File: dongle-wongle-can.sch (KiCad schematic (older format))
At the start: 33 parts

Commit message: updated project layout
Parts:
- removed U?: AP1509-33, symbol star-sch-block-symbols:AP1509-33
- added U?: AP1509-33, symbol hardware-sch-blocks:AP1509-33
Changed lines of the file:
@@
 Text Notes 6350 3050 0    50   ~ 0
 POWER
-Wire Wire Line
-	6800 4750 7100 4750
 $Comp
-L star-sch-block-symbols:AP1509-33 U?
-U 1 1 5F0A0CB9
+L hardware-sch-blocks:AP1509-33 U?
+U 1 1 5EA62ACD
 P 7300 4300
 F 0 "U?" H 7744 4271 50  0000 L CNN
@@
 $EndComp
 Wire Wire Line
+	6800 4750 7100 4750
+Wire Wire Line
 	7500 4750 7800 4750
-Wire Wire Line
-	7500 4750 7400 4750
-Connection ~ 7500 4750
-Wire Wire Line
-	7400 4750 7300 4750
-Connection ~ 7400 4750
 Wire Wire Line
 	7100 4750 7200 4750
 Connection ~ 7100 4750
+Wire Wire Line
+	7200 4750 7300 4750
 Connection ~ 7200 4750
 Wire Wire Line
-	7200 4750 7300 4750
+	7300 4750 7400 4750
 Connection ~ 7300 4750
+Wire Wire Line
+	7400 4750 7500 4750
+Connection ~ 7400 4750
+Connection ~ 7500 4750
 $EndSCHEMATC

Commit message: updated footprints
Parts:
- C1, C2, C3, C4, C5, C6, C7: renamed from C?; footprint (none) -> Capacitor_SMD:C_0603_1608Metric
- D1: renamed from D?; footprint (none) -> Diode_SMD:D_0603_1608Metric
- D2: renamed from D?; footprint (none) -> LED_SMD:LED_0603_1608Metric_Castellated
- J1: renamed from J?; footprint (none) -> hardware-sch-blocks:505448-0871
- J2, J3: renamed from J?; footprint (none) -> Connector_PinHeader_2.54mm:PinHeader_1x12_P2.54mm_Vertical
- J4: renamed from J?; footprint (none) -> hardware-sch-blocks:TSM-103-01-L-SV
- J5: renamed from J?; footprint (none) -> hardware-sch-blocks:FTMH-120-03-F-DV-P
- JP1: renamed from JP?; footprint (none) -> Jumper:SolderJumper-2_P1.3mm_Open_Pad1.0x1.5mm
- JP2, JP3, JP4: renamed from JP?; footprint (none) -> Jumper:SolderJumper-3_P1.3mm_Bridged2Bar12_Pad1.0x1.5mm
- L1: renamed from L?; footprint (none) -> Inductor_SMD:L_0603_1608Metric
- R1, R2, R3, R4, R5, R6: renamed from R?; footprint (none) -> Resistor_SMD:R_0603_1608Metric
- RN1: renamed from RN?; footprint (none) -> Resistor_SMD:R_Array_Concave_4x0603
- RN2: renamed from RN?; footprint (none) -> Resistor_SMD:R_Array_Concave_2x0603
- SW1: renamed from SW?; footprint (none) -> Button_Switch_SMD:SW_SPST_CK_RS282G05A3
- TP1, TP2: renamed from TP?; footprint (none) -> TestPoint:TestPoint_Keystone_5005-5009_Compact
- U3: renamed from U?; footprint (none) -> Package_SO:SOIC-8_3.9x4.9mm_P1.27mm
- gave numbers to parts that had none: 2
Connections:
- net VDD: now also C7.1
- net at C6.2, D1.2 (A), U3.4 (SD)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: now also C7.2
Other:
- moved on the sheet: C7

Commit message: add layout
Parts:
- removed J2: PROTO_IO, Connector_PinHeader_2.54mm:PinHeader_1x12_P2.54mm_Vertical, symbol Connector_Generic:Conn_02x06_Counter_Clockwise
- removed J3: PROTO_POWER, Connector_PinHeader_2.54mm:PinHeader_1x12_P2.54mm_Vertical, symbol Connector_Generic:Conn_02x06_Counter_Clockwise
- removed JP1: BOOT_JUMP, Jumper:SolderJumper-2_P1.3mm_Open_Pad1.0x1.5mm, symbol Jumper:SolderJumper_2_Open
- removed TP1: CANH_TP, TestPoint:TestPoint_Keystone_5005-5009_Compact, symbol Connector:TestPoint
- removed TP2: CANL_TP, TestPoint:TestPoint_Keystone_5005-5009_Compact, symbol Connector:TestPoint
- added H1, H2, H3, H4: MountingHole, MountingHole:MountingHole_3mm, symbol Mechanical:MountingHole
- added J2: PROTO_IO, Connector_PinHeader_2.54mm:PinHeader_2x06_P2.54mm_Vertical, symbol Connector_Generic:Conn_02x06_Odd_Even
- added J3: PROTO_PWR, hardware-sch-blocks:PROTO_2x6, symbol Connector_Generic:Conn_02x06_Odd_Even
- added J6: PROTO1, hardware-sch-blocks:PROTO_2x6, symbol Connector_Generic:Conn_02x06_Odd_Even
- added J7: PROTO2, hardware-sch-blocks:PROTO_2x6, symbol Connector_Generic:Conn_02x06_Odd_Even
- J5: footprint hardware-sch-blocks:FTMH-120-03-F-DV-P -> hardware-sch-blocks:FTSH-105-01-L-DV-K
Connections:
- net CAN_RX: now also R2.2
- net GND: now also C6.2, C7.2, D1.2 (A), U3.4 (SD), U3.5 (GND), U3.6 (GND), U3.7 (GND), U3.8 (GND), J3.1 (Pin_1), J3.11 (Pin_11), J3.3 (Pin_3), J3.5 (Pin_5), J3.7 (Pin_7), J3.9 (Pin_9)
- net GPIO0: now also J2.2 (Pin_2)
- net GPIO1: now also J2.1 (Pin_1)
- net I2C_SCL: now also J2.8 (Pin_8)
- net I2C_SDA: now also J2.10 (Pin_10)
- net SWDCLK: now also J2.11 (Pin_11)
- net SWDIO: now also J2.12 (Pin_12)
- net UART_RX: now also J2.4 (Pin_4)
- net UART_TX: now also J2.6 (Pin_6)
- net VDD: now also J3.10 (Pin_10), J3.12 (Pin_12), J3.2 (Pin_2), J3.4 (Pin_4), J3.6 (Pin_6), J3.8 (Pin_8)
- net at RN1.5 (R4.2): now also J2.9 (Pin_9)
- net at RN1.6 (R3.2): now also J2.7 (Pin_7)
- net at RN1.7 (R2.2): now also J2.5 (Pin_5)
- net at RN1.8 (R1.2): now also J2.3 (Pin_3)
- no-connect marks 2 -> 26
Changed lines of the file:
@@
 F 0 "J5" H 5700 6700 50  0000 R CNN
 F 1 "Conn_ARM_JTAG_SWD_10" V 5550 6600 50  0000 R CNN
-F 2 "hardware-sch-blocks:FTMH-120-03-F-DV-P" H 6000 6150 50  0001 C CNN
+F 2 "hardware-sch-blocks:FTSH-105-01-L-DV-K" H 6000 6150 50  0001 C CNN
 F 3 "http://infocenter.arm.com/help/topic/com.arm.doc.ddi0314h/DDI0314H_coresight_components_trm.pdf" V 5650 4900 50  0001 C CNN
 	1    6000 6150
@@
 Text GLabel 1600 4550 2    50   Input ~ 0
 CANL
-Wire Wire Line
-	1100 4600 1100 4550
 Wire Wire Line
 	1100 4300 1100 4250
@@
 Wire Wire Line
 	7450 3700 7600 3700
-$Comp
-L Connector:TestPoint TP1
-U 1 1 5EB87845
-P 1100 4200
-F 0 "TP1" H 1158 4318 50  0000 L CNN
-F 1 "CANH_TP" H 1158 4227 50  0000 L CNN
-F 2 "TestPoint:TestPoint_Keystone_5005-5009_Compact" H 1300 4200 50  0001 C CNN
-F 3 "~" H 1300 4200 50  0001 C CNN
-	1    1100 4200
-	1    0    0    -1
-$EndComp
-$Comp
-L Connector:TestPoint TP2
-U 1 1 5EB8AE14
-P 1100 4600
-F 0 "TP2" H 1042 4626 50  0000 R CNN
-F 1 "CANL_TP" H 1042 4717 50  0000 R CNN
-F 2 "TestPoint:TestPoint_Keystone_5005-5009_Compact" H 1300 4600 50  0001 C CNN
-F 3 "~" H 1300 4600 50  0001 C CNN
-	1    1100 4600
-	-1   0    0    1
-$EndComp
 Wire Wire Line
 	1100 4550 1600 4550
-Connection ~ 1100 4550
 Wire Wire Line
 	1100 4550 1100 4500
 Wire Wire Line
 	1600 4250 1100 4250
-Connection ~ 1100 4250
-Wire Wire Line
-	1100 4250 1100 4200
 $Comp
 L Device:C_Small C2
@@
 $EndComp
 Wire Wire Line
-	1200 7300 1350 7300
-Wire Wire Line
 	1000 7300 900  7300
-Wire Wire Line
-	1650 7300 1750 7300
 Wire Wire Line
 	1750 7300 1750 7050
 Connection ~ 1750 7050
-$Comp
-L Jumper:SolderJumper_2_Open JP1
-U 1 1 5EC6FD0B
-P 1500 7300
-F 0 "JP1" H 1500 7200 50  0000 C CNN
-F 1 "BOOT_JUMP" H 1500 7414 50  0000 C CNN
-F 2 "Jumper:SolderJumper-2_P1.3mm_Open_Pad1.0x1.5mm" H 1500 7300 50  0001 C CNN
-F 3 "~" H 1500 7300 50  0001 C CNN
-	1    1500 7300
-	1    0    0    -1
-$EndComp
-$Comp
-L Connector_Generic:Conn_02x06_Counter_Clockwise J3
-U 1 1 5ECB63F8
-P 3550 2050
-F 0 "J3" H 3600 2467 50  0000 C CNN
-F 1 "PROTO_POWER" H 3600 2376 50  0000 C CNN
-F 2 "Connector_PinHeader_2.54mm:PinHeader_1x12_P2.54mm_Vertical" H 3550 2050 50  0001 C CNN
-F 3 "~" H 3550 2050 50  0001 C CNN
-	1    3550 2050
-	1    0    0    -1
-$EndComp
 $Comp
 L power:GND #PWR0125
@@
 Text GLabel 1300 2350 0    50   Input ~ 0
 SWDCLK
-$Comp
-L Connector_Generic:Conn_02x06_Counter_Clockwise J2
-U 1 1 5ECFB1DE
-P 2200 2050
-F 0 "J2" H 2250 2467 50  0000 C CNN
-F 1 "PROTO_IO" H 2250 2376 50  0000 C CNN
-F 2 "Connector_PinHeader_2.54mm:PinHeader_1x12_P2.54mm_Vertical" H 2200 2050 50  0001 C CNN
-F 3 "~" H 2200 2050 50  0001 C CNN
-	1    2200 2050
-	1    0    0    -1
-$EndComp
 Wire Wire Line
 	2650 2350 2500 2350
@@
 Wire Notes Line
 	750  2700 750  1550
-Wire Notes Line
-	750  1550 4150 1550
-Wire Notes Line
-	4150 1550 4150 2700
-Wire Notes Line
-	4150 2700 750  2700
 Text Notes 800  1700 0    100  ~ 0
 PROTO AREA\n
@@
 	8350 4750 7800 4750
 Connection ~ 7800 4750
+$Comp
+L Connector_Generic:Conn_02x06_Odd_Even J2
+U 1 1 5EAA4304
+P 2200 2050
+F 0 "J2" H 2250 2467 50  0000 C CNN
+F 1 "PROTO_IO" H 2250 2376 50  0000 C CNN
+F 2 "Connector_PinHeader_2.54mm:PinHeader_2x06_P2.54mm_Vertical" H 2200 2050 50  0001 C CNN
+F 3 "~" H 2200 2050 50  0001 C CNN
+	1    2200 2050
+	1    0    0    -1
+$EndComp
+$Comp
+L Connector_Generic:Conn_02x06_Odd_Even J3
+U 1 1 5EAA4D80
+P 3550 2050
+F 0 "J3" H 3600 2467 50  0000 C CNN
+F 1 "PROTO_PWR" H 3600 2376 50  0000 C CNN
+F 2 "hardware-sch-blocks:PROTO_2x6" H 3550 2050 50  0001 C CNN
+F 3 "~" H 3550 2050 50  0001 C CNN
+	1    3550 2050
+	1    0    0    -1
+$EndComp
+$Comp
+L power:GND #PWR0129
+U 1 1 5EAEA6ED
+P 8600 4750
+F 0 "#PWR0129" H 8600 4500 50  0001 C CNN
+F 1 "GND" H 8750 4750 50  0000 C CNN
+F 2 "" H 8600 4750 50  0001 C CNN
+F 3 "" H 8600 4750 50  0001 C CNN
+	1    8600 4750
+	1    0    0    -1
+$EndComp
+Wire Wire Line
+	8600 4750 8350 4750
+Connection ~ 8350 4750
+$Comp
+L Mechanical:MountingHole H1
+U 1 1 5EAF5044
+P 6450 3250
+F 0 "H1" H 6550 3296 50  0000 L CNN
+F 1 "MountingHole" H 6550 3205 50  0000 L CNN
+F 2 "MountingHole:MountingHole_3mm" H 6450 3250 50  0001 C CNN
+F 3 "~" H 6450 3250 50  0001 C CNN
+	1    6450 3250
+	1    0    0    -1
+$EndComp
+$Comp
+L Mechanical:MountingHole H2
+U 1 1 5EAF76F6
+P 6450 3450
+F 0 "H2" H 6550 3496 50  0000 L CNN
+F 1 "MountingHole" H 6550 3405 50  0000 L CNN
+F 2 "MountingHole:MountingHole_3mm" H 6450 3450 50  0001 C CNN
+F 3 "~" H 6450 3450 50  0001 C CNN
+	1    6450 3450
+	1    0    0    -1
+$EndComp
+$Comp
+L Mechanical:MountingHole H3
+U 1 1 5EAF7A66
+P 6450 3650
+F 0 "H3" H 6550 3696 50  0000 L CNN
+F 1 "MountingHole" H 6550 3605 50  0000 L CNN
+F 2 "MountingHole:MountingHole_3mm" H 6450 3650 50  0001 C CNN
+F 3 "~" H 6450 3650 50  0001 C CNN
+	1    6450 3650
+	1    0    0    -1
+$EndComp
+$Comp
+L Mechanical:MountingHole H4
+U 1 1 5EAF7F60
+P 6450 3850
+F 0 "H4" H 6550 3896 50  0000 L CNN
+F 1 "MountingHole" H 6550 3805 50  0000 L CNN
+F 2 "MountingHole:MountingHole_3mm" H 6450 3850 50  0001 C CNN
+F 3 "~" H 6450 3850 50  0001 C CNN
+	1    6450 3850
+	1    0    0    -1
+$EndComp
+Wire Wire Line
+	1200 7300 1750 7300
+$Comp
+L Connector_Generic:Conn_02x06_Odd_Even J6
+U 1 1 5EB575D3
+P 4500 2050
+F 0 "J6" H 4550 2467 50  0000 C CNN
+F 1 "PROTO1" H 4550 2376 50  0000 C CNN
+F 2 "hardware-sch-blocks:PROTO_2x6" H 4500 2050 50  0001 C CNN
+F 3 "~" H 4500 2050 50  0001 C CNN
+	1    4500 2050
+	1    0    0    -1
+$EndComp
+$Comp
+L Connector_Generic:Conn_02x06_Odd_Even J7
+U 1 1 5EB5846C
+P 5350 2050
+F 0 "J7" H 5400 2467 50  0000 C CNN
+F 1 "PROTO2" H 5400 2376 50  0000 C CNN
+F 2 "hardware-sch-blocks:PROTO_2x6" H 5350 2050 50  0001 C CNN
+F 3 "~" H 5350 2050 50  0001 C CNN
+	1    5350 2050
+	1    0    0    -1
+$EndComp
+NoConn ~ 4300 1850
+NoConn ~ 4300 1950
+NoConn ~ 4300 2050
+NoConn ~ 4300 2150
+NoConn ~ 4300 2250
+NoConn ~ 4300 2350
+NoConn ~ 4800 2350
+NoConn ~ 4800 2250
+NoConn ~ 4800 2150
+NoConn ~ 4800 2050
+NoConn ~ 4800 1950
+NoConn ~ 4800 1850
+NoConn ~ 5150 1850
+NoConn ~ 5150 1950
+NoConn ~ 5150 2050
+NoConn ~ 5150 2150
+NoConn ~ 5150 2250
+NoConn ~ 5150 2350
+NoConn ~ 5650 2350
+NoConn ~ 5650 2250
+NoConn ~ 5650 2150
+NoConn ~ 5650 2050
+NoConn ~ 5650 1950
+NoConn ~ 5650 1850
+Wire Notes Line
+	6050 2700 6050 1550
+Wire Notes Line
+	750  1550 6050 1550
+Wire Notes Line
+	750  2700 6050 2700
 $EndSCHEMATC

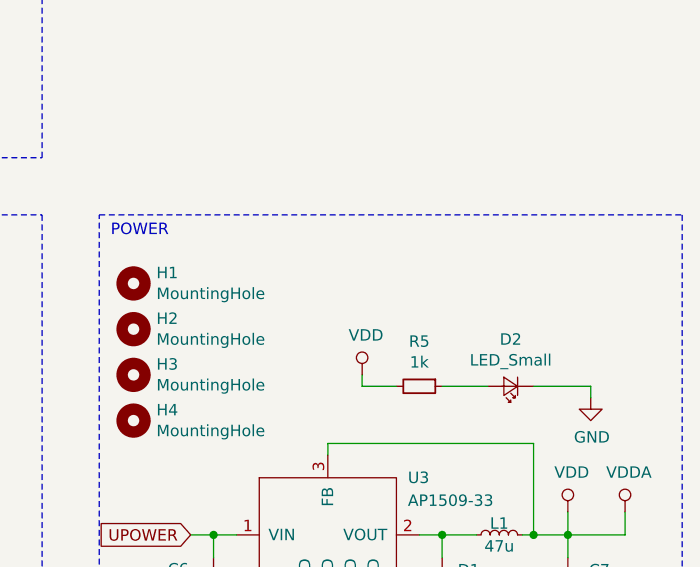
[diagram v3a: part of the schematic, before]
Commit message: make silk 10/10 and add some art
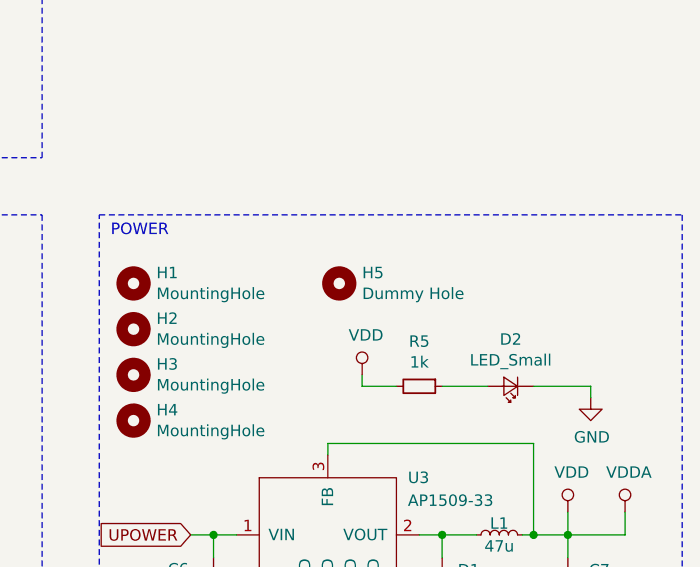
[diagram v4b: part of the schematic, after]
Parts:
- added H5: Dummy Hole, hardware-sch-blocks:airbears, symbol Mechanical:MountingHole
- J2: footprint Connector_PinHeader_2.54mm:PinHeader_2x06_P2.54mm_Vertical -> hardware-sch-blocks:PROTO_2x6
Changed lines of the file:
@@
 F 0 "J2" H 2250 2467 50  0000 C CNN
 F 1 "PROTO_IO" H 2250 2376 50  0000 C CNN
-F 2 "Connector_PinHeader_2.54mm:PinHeader_2x06_P2.54mm_Vertical" H 2200 2050 50  0001 C CNN
+F 2 "hardware-sch-blocks:PROTO_2x6" H 2200 2050 50  0001 C CNN
 F 3 "~" H 2200 2050 50  0001 C CNN
 	1    2200 2050
@@
 Wire Notes Line
 	750  2700 6050 2700
+$Comp
+L Mechanical:MountingHole H5
+U 1 1 5EA863C0
+P 7350 3250
+F 0 "H5" H 7450 3296 50  0000 L CNN
+F 1 "Dummy Hole" H 7450 3205 50  0000 L CNN
+F 2 "hardware-sch-blocks:airbears" H 7350 3250 50  0001 C CNN
+F 3 "~" H 7350 3250 50  0001 C CNN
+	1    7350 3250
+	1    0    0    -1
+$EndComp
 $EndSCHEMATC

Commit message: change resistor pack footprints
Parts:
- C1: mfn# (none) -> C0603C103M5RACTU
- C2: mfn# (none) -> C0603C104Z3VACTU
- C3: mfn# (none) -> CL10A105KP8NNNC
- C4, C5: mfn# (none) -> CC0603MRX5R6BB475
- C6, C7: mfn# (none) -> GRM188R6YA106MA73D
- D1: mfn# (none) -> CDBU0340-HF
- D2: mfn# (none) -> 150060GS75000
- J1: mfn# (none) -> 5054480871
- J4: mfn# (none) -> TSM-103-01-L-SV
- J5: mfn# (none) -> FTSH-105-01-L-DV-K-TR
- L1: mfn# (none) -> LBMF1608T470K
- R1: mfn# (none) -> RC0603FR-07120RL
- R2, R3, R5, R6: mfn# (none) -> RC0603JR-071KL
- R4: mfn# (none) -> RC0603JR-0710KL
- RN1: footprint Resistor_SMD:R_Array_Concave_4x0603 -> Resistor_SMD:R_Array_Convex_4x1206; mfn# (none) -> 742C083000XP
- RN2: value 200 -> 330; footprint Resistor_SMD:R_Array_Concave_2x0603 -> Resistor_SMD:R_Array_Convex_2x0606; mfn# (none) -> EXB-34V331JV
- SW1: mfn# (none) -> RS-282G05A3-SM RT
- U1: mfn# (none) -> STM32F042F6P6TR
- U2: mfn# (none) -> SN65HVD233DR
- U3: mfn# (none) -> AP1509-33SG-13
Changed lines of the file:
@@
 F 2 "Package_SO:TSSOP-20_4.4x6.5mm_P0.65mm" H 1850 5750 50  0001 R CNN
 F 3 "http://www.st.com/st-web-ui/static/active/en/resource/technical/document/datasheet/DM00105814.pdf" H 2350 6450 50  0001 C CNN
+F 4 "STM32F042F6P6TR" H 2350 6450 50  0001 C CNN "mfn#"
 	1    2350 6450
 	1    0    0    -1
@@
 F 2 "hardware-sch-blocks:FTSH-105-01-L-DV-K" H 6000 6150 50  0001 C CNN
 F 3 "http://infocenter.arm.com/help/topic/com.arm.doc.ddi0314h/DDI0314H_coresight_components_trm.pdf" V 5650 4900 50  0001 C CNN
+F 4 "FTSH-105-01-L-DV-K-TR" H 6000 6150 50  0001 C CNN "mfn#"
 	1    6000 6150
 	1    0    0    -1
@@
 F 1 "1K" H 8109 5705 50  0000 L CNN
 F 2 "Resistor_SMD:R_0603_1608Metric" H 8050 5750 50  0001 C CNN
-F 3 "~" H 8050 5750 50  0001 C CNN
+F 3 "" H 8050 5750 50  0001 C CNN
+F 4 "RC0603JR-071KL" H 8050 5750 50  0001 C CNN "mfn#"
 	1    8050 5750
 	1    0    0    -1
@@
 F 2 "Button_Switch_SMD:SW_SPST_CK_RS282G05A3" H 7700 6100 50  0001 C CNN
 F 3 "~" H 7700 6100 50  0001 C CNN
+F 4 "RS-282G05A3-SM RT" H 7700 5900 50  0001 C CNN "mfn#"
 	1    7700 5900
 	1    0    0    -1
@@
 F 2 "hardware-sch-blocks:505448-0871" H 1800 3500 50  0001 C CNN
 F 3 "~" H 1800 3500 50  0001 C CNN
+F 4 "5054480871" H 1800 3500 50  0001 C CNN "mfn#"
 	1    1800 3500
 	1    0    0    -1
@@
 F 2 "Package_SO:SOIC-8_3.9x4.9mm_P1.27mm" H 3900 3000 50  0001 C CNN
 F 3 "http://www.ti.com/lit/ds/symlink/sn65hvd234.pdf" H 3800 3900 50  0001 C CNN
+F 4 "SN65HVD233DR" H 3900 3500 50  0001 C CNN "mfn#"
 	1    3900 3500
 	1    0    0    -1
@@
 F 2 "Capacitor_SMD:C_0603_1608Metric" H 4950 3550 50  0001 C CNN
 F 3 "~" H 4950 3550 50  0001 C CNN
+F 4 "CC0603MRX5R6BB475" H 4950 3550 50  0001 C CNN "mfn#"
 	1    4950 3550
 	1    0    0    -1
@@
 F 2 "Resistor_SMD:R_0603_1608Metric" H 1100 4400 50  0001 C CNN
 F 3 "~" H 1100 4400 50  0001 C CNN
+F 4 "RC0603FR-07120RL" H 1100 4400 50  0001 C CNN "mfn#"
 	1    1100 4400
 	1    0    0    -1
@@
 F 2 "Resistor_SMD:R_0603_1608Metric" H 4500 4400 50  0001 C CNN
 F 3 "~" H 4500 4400 50  0001 C CNN
+F 4 "RC0603JR-0710KL" V 4500 4400 50  0001 C CNN "mfn#"
 	1    4500 4400
 	0    1    1    0
@@
 F 2 "Resistor_SMD:R_0603_1608Metric" H 3150 4100 50  0001 C CNN
 F 3 "~" H 3150 4100 50  0001 C CNN
+F 4 "RC0603JR-071KL" V 3150 4100 50  0001 C CNN "mfn#"
 	1    3150 4100
 	0    1    1    0
@@
 P 3800 6250
 F 0 "RN2" V 3900 6250 50  0000 C CNN
-F 1 "200" V 4000 6250 50  0000 C CNN
-F 2 "Resistor_SMD:R_Array_Concave_2x0603" V 3975 6250 50  0001 C CNN
+F 1 "330" V 4000 6250 50  0000 C CNN
+F 2 "Resistor_SMD:R_Array_Convex_2x0606" V 3975 6250 50  0001 C CNN
 F 3 "~" H 3800 6250 50  0001 C CNN
+F 4 "EXB-34V331JV" V 3800 6250 50  0001 C CNN "mfn#"
 	1    3800 6250
 	0    1    1    0
@@
 F 0 "RN1" V 1850 2150 50  0000 C CNN
 F 1 "0" V 1950 2150 50  0000 C CNN
-F 2 "Resistor_SMD:R_Array_Concave_4x0603" V 1925 2150 50  0001 C CNN
+F 2 "Resistor_SMD:R_Array_Convex_4x1206" V 1925 2150 50  0001 C CNN
 F 3 "~" H 1650 2150 50  0001 C CNN
+F 4 "742C083000XP" V 1650 2150 50  0001 C CNN "mfn#"
 	1    1650 2150
 	0    1    1    0
@@
 F 2 "hardware-sch-blocks:TSM-103-01-L-SV" H 5450 7300 50  0001 C CNN
 F 3 "~" H 5450 7300 50  0001 C CNN
+F 4 "TSM-103-01-L-SV" H 5450 7300 50  0001 C CNN "mfn#"
 	1    5450 7300
 	1    0    0    -1
@@
 F 2 "Resistor_SMD:R_0603_1608Metric" H 7700 3700 50  0001 C CNN
 F 3 "~" H 7700 3700 50  0001 C CNN
+F 4 "RC0603JR-071KL" V 7700 3700 50  0001 C CNN "mfn#"
 	1    7700 3700
 	0    1    1    0
@@
 F 2 "LED_SMD:LED_0603_1608Metric_Castellated" V 8100 3700 50  0001 C CNN
 F 3 "~" V 8100 3700 50  0001 C CNN
+F 4 "150060GS75000" H 8100 3700 50  0001 C CNN "mfn#"
 	1    8100 3700
 	-1   0    0    1
@@
 F 2 "Capacitor_SMD:C_0603_1608Metric" H 4000 7200 50  0001 C CNN
 F 3 "~" H 4000 7200 50  0001 C CNN
+F 4 "C0603C104Z3VACTU" H 4000 7200 50  0001 C CNN "mfn#"
 	1    4000 7200
 	1    0    0    -1
@@
 F 2 "Capacitor_SMD:C_0603_1608Metric" H 4400 7200 50  0001 C CNN
 F 3 "~" H 4400 7200 50  0001 C CNN
+F 4 "CC0603MRX5R6BB475" H 4400 7200 50  0001 C CNN "mfn#"
 	1    4400 7200
 	1    0    0    -1
@@
 F 2 "Capacitor_SMD:C_0603_1608Metric" H 3950 5550 50  0001 C CNN
 F 3 "~" H 3950 5550 50  0001 C CNN
+F 4 "C0603C103M5RACTU" H 3950 5550 50  0001 C CNN "mfn#"
 	1    3950 5550
 	1    0    0    -1
@@
 F 2 "Capacitor_SMD:C_0603_1608Metric" H 4350 5550 50  0001 C CNN
 F 3 "~" H 4350 5550 50  0001 C CNN
+F 4 "CL10A105KP8NNNC" H 4350 5550 50  0001 C CNN "mfn#"
 	1    4350 5550
 	1    0    0    -1
@@
 F 2 "Resistor_SMD:R_0603_1608Metric" H 1100 7300 50  0001 C CNN
 F 3 "~" H 1100 7300 50  0001 C CNN
+F 4 "RC0603JR-071KL" H 1100 7300 50  0001 C CNN "mfn#"
 	1    1100 7300
 	0    -1   -1   0
@@
 F 2 "Inductor_SMD:L_0603_1608Metric" H 8050 4350 50  0001 C CNN
 F 3 "~" H 8050 4350 50  0001 C CNN
+F 4 "LBMF1608T470K" H 8050 4350 50  0001 C CNN "mfn#"
 	1    8050 4350
 	0    -1   -1   0
@@
 F 2 "Diode_SMD:D_0603_1608Metric" V 7800 4550 50  0001 C CNN
 F 3 "~" V 7800 4550 50  0001 C CNN
+F 4 "CDBU0340-HF" H 7800 4550 50  0001 C CNN "mfn#"
 	1    7800 4550
 	0    1    1    0
@@
 F 2 "Capacitor_SMD:C_0603_1608Metric" H 8350 4550 50  0001 C CNN
 F 3 "~" H 8350 4550 50  0001 C CNN
+F 4 "GRM188R6YA106MA73D" H 8350 4550 50  0001 C CNN "mfn#"
 	1    8350 4550
 	1    0    0    -1
@@
 F 2 "Capacitor_SMD:C_0603_1608Metric" H 6800 4550 50  0001 C CNN
 F 3 "~" H 6800 4550 50  0001 C CNN
+F 4 "GRM188R6YA106MA73D" H 6800 4550 50  0001 C CNN "mfn#"
 	1    6800 4550
 	1    0    0    -1
@@
 F 2 "Package_SO:SOIC-8_3.9x4.9mm_P1.27mm" H 7350 4650 50  0001 C CNN
 F 3 "https://www.diodes.com/assets/Datasheets/AP1509.pdf" H 7350 4650 50  0001 C CNN
+F 4 "AP1509-33SG-13" H 7300 4300 50  0001 C CNN "mfn#"
 	1    7300 4300
 	1    0    0    -1
